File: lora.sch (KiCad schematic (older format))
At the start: 30 parts

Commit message: minor updates
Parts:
- removed J?: Program, symbol Connector_Generic:Conn_01x04
- removed U?: AZ1117-3.3, symbol Regulator_Linear:AZ1117-3.3
- added C?: 12p, Capacitor_SMD:C_0603_1608Metric, symbol Device:C_Small
- added J?: Temp, symbol Connector_Generic:Conn_01x03
- added R? (x2): 10k, symbol Device:R_Small
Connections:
- net labels added: RTC_IRQ
- wire segments 22 -> 31
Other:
- note added: "1.8V - 3.9V"
- note added: "1.8V - 5.5V"
- note added: "3.0V - 3.6V"
- note added: "3.5V Buck converter > 2.5A ! Not needed in battery mode!"
- note added: "SIM800 requires up to 2A in burst mode and 3.4V to 4.4V"
- note added: "UBLOX Neo 6: 2.7 - 3.6V"
- note removed: "Achtung 3.3V laut Datenblatt nicht ausreichend. \n"
- note removed: "Brauchen wir die anderen DIO1-5 wirklich nicht?"
- note removed: "Eingang Edge Interruptfähig?"
- note removed: "Ist 32D wirkich der Richtige? \nDa gibt es auch noch andere Endbuchstaben."
- moved on the sheet: J?

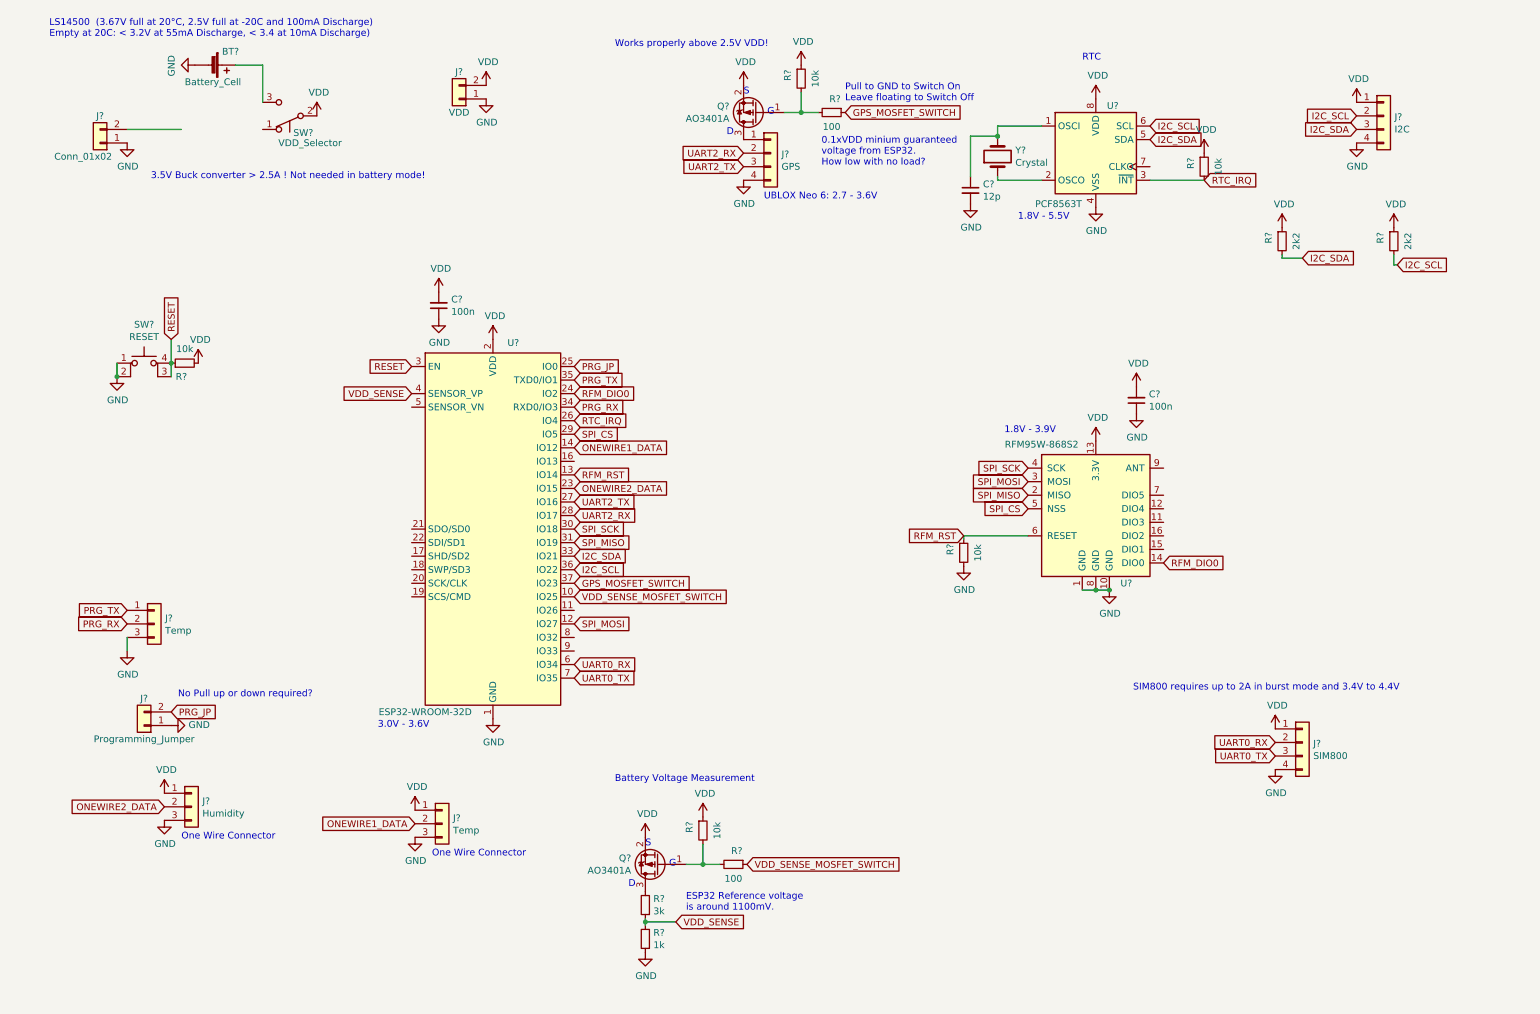
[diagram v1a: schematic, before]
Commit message: finished dc dc power supply.
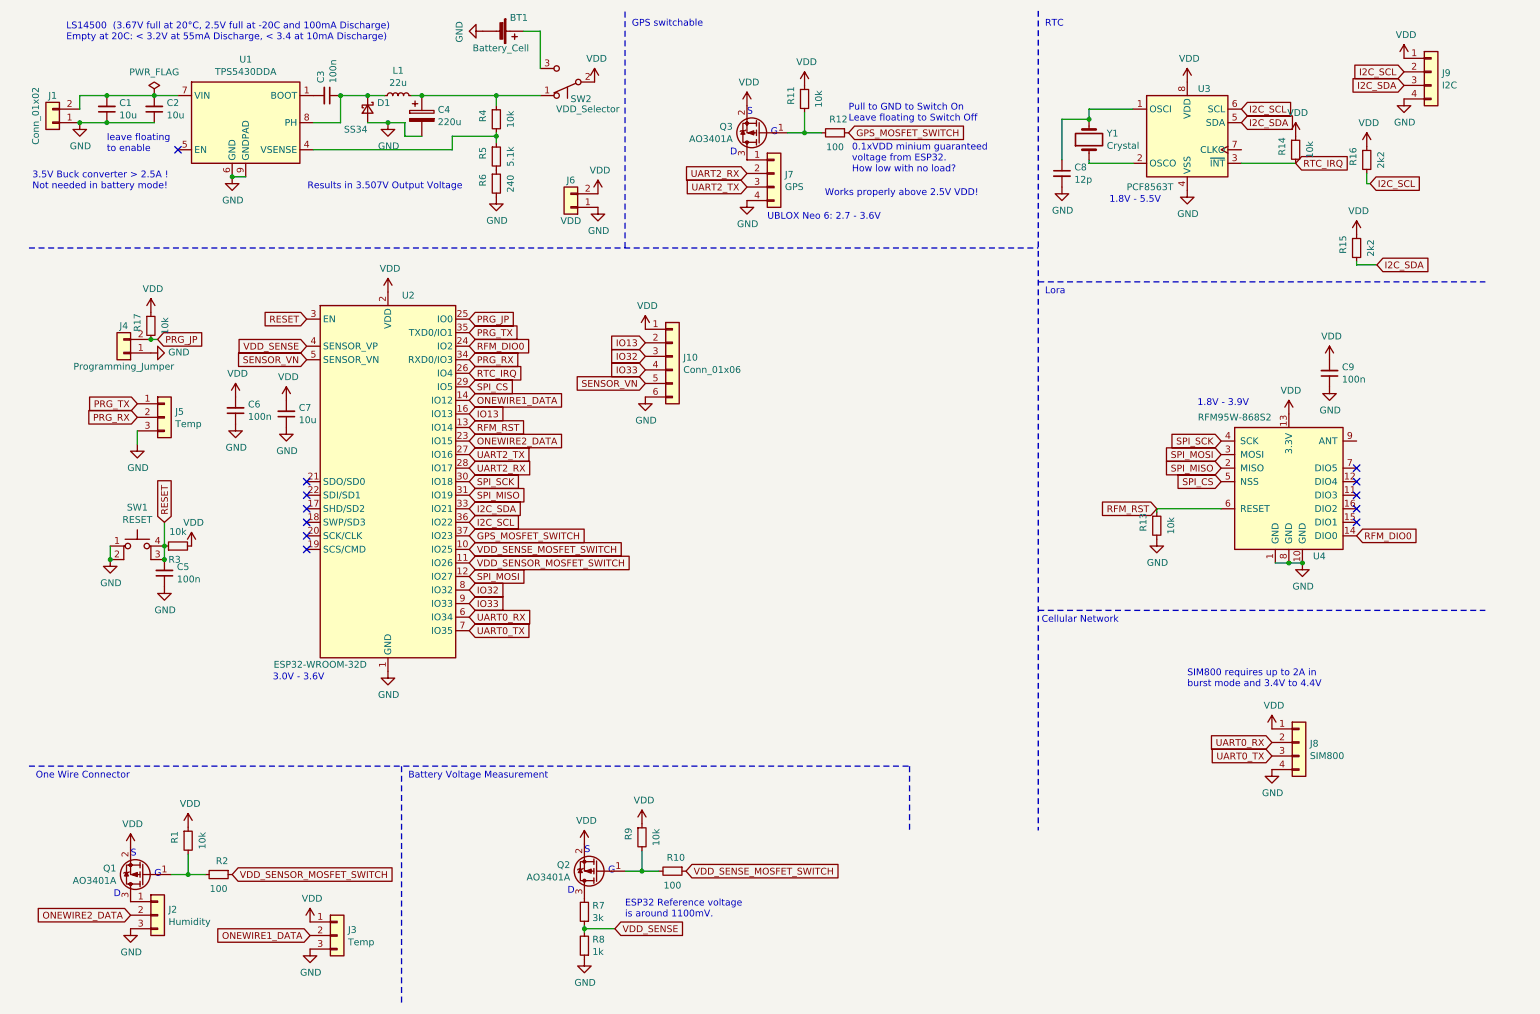
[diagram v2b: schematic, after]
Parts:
- added C1, C2, C7: 10u, symbol Device:C_Small
- added C3, C5: 100n, symbol Device:C_Small
- added C4: 220u, Capacitor_SMD:CP_Elec_6.3x7.7, symbol Device:CP
- added D1: SS34, symbol Device:D_Schottky_Small
- added J10: Conn_01x06, symbol Connector_Generic:Conn_01x06
- added L1: 22u, symbol Device:L_Small
- added Q1: AO3401A, Package_TO_SOT_SMD:SOT-23, symbol Transistor_FET:AO3401A
- added R1, R17, R4: 10k, symbol Device:R_Small
- added R2: 100, symbol Device:R_Small
- added R5: 5.1k, Resistor_SMD:R_0603_1608Metric, symbol Device:R_Small
- added R6: 240, Resistor_SMD:R_0603_1608Metric, symbol Device:R_Small
- added U1: TPS5430DDA, Package_SO:TI_SO-PowerPAD-8_ThermalVias, symbol Regulator_Switching:TPS5430DDA
- gave numbers to parts that had none: 32
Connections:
- net labels added: IO13, IO32, IO33, SENSOR_VN, VDD_SENSOR_MOSFET_SWITCH
- wire segments 31 -> 58
- no-connect marks 0 -> 12
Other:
- note added: "3.5V Buck converter > 2.5A !\nNot needed in battery mode!"
- note added: "Cellular Network"
- note added: "GPS switchable"
- note added: "Lora"
- note added: "Results in 3.507V Output Voltage"
- note added: "SIM800 requires up to 2A in \nburst mode and 3.4V to 4.4V"
- note added: "leave floating\nto enable"
- note removed: "3.5V Buck converter > 2.5A ! Not needed in battery mode!"
- note removed: "No Pull up or down required?"
- note removed: "SIM800 requires up to 2A in burst mode and 3.4V to 4.4V"
- moved on the sheet: BT1, C6, C8, C9, J1, J2, J3, J4, J5, J6, J7, J8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

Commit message: nothing major
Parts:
- added J11: Conn_Coaxial, symbol Connector:Conn_Coaxial
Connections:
- net GND: now also J11.2 (Ext)
- net at U4.9 (ANT): now also J11.1 (In)
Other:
- note added: "SMA or just a\nsimple short wire"
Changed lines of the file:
@@
 	1    0    0    -1
 $EndComp
+$Comp
+L Connector:Conn_Coaxial J11
+U 1 1 5FC31EE2
+P 10475 3650
+F 0 "J11" H 10575 3625 50  0000 L CNN
+F 1 "Conn_Coaxial" H 10575 3534 50  0000 L CNN
+F 2 "" H 10475 3650 50  0001 C CNN
+F 3 " ~" H 10475 3650 50  0001 C CNN
+	1    10475 3650
+	1    0    0    -1
+$EndComp
+$Comp
+L power:GND #PWR0146
+U 1 1 5FC3451D
+P 10475 3850
+F 0 "#PWR0146" H 10475 3600 50  0001 C CNN
+F 1 "GND" H 10480 3677 50  0000 C CNN
+F 2 "" H 10475 3850 50  0001 C CNN
+F 3 "" H 10475 3850 50  0001 C CNN
+	1    10475 3850
+	1    0    0    -1
+$EndComp
+Text Notes 10275 3500 0    50   ~ 0
+SMA or just a\nsimple short wire
 $EndSCHEMATC

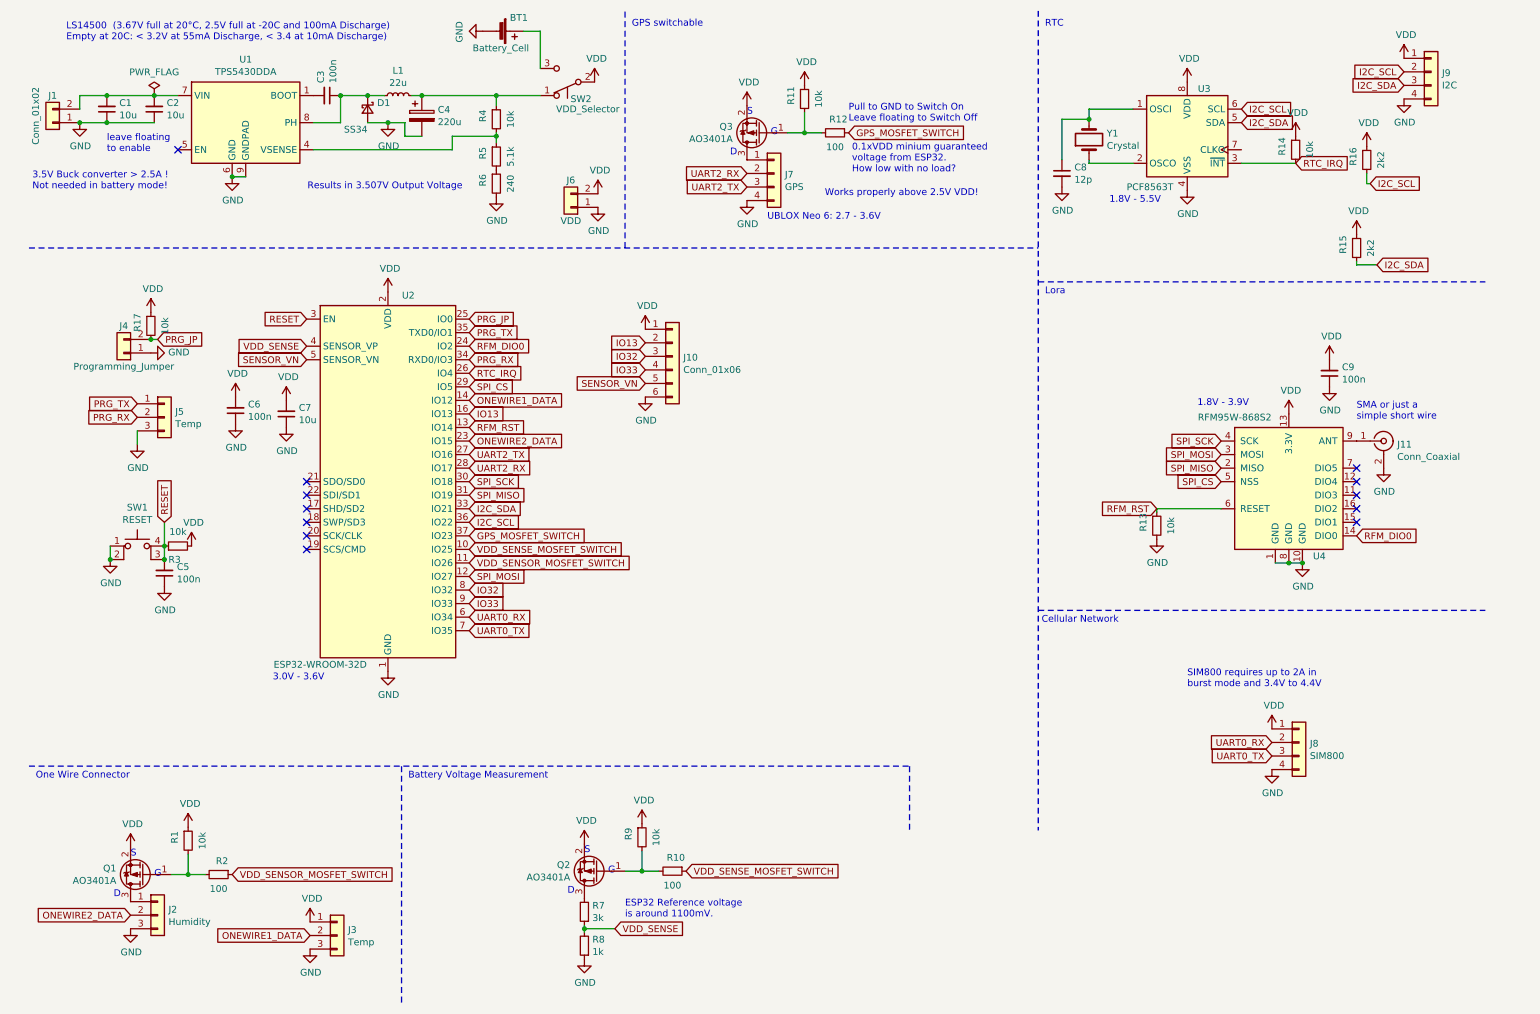
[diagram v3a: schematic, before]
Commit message: removed RTC, added 32KHZ crystal to esp32.
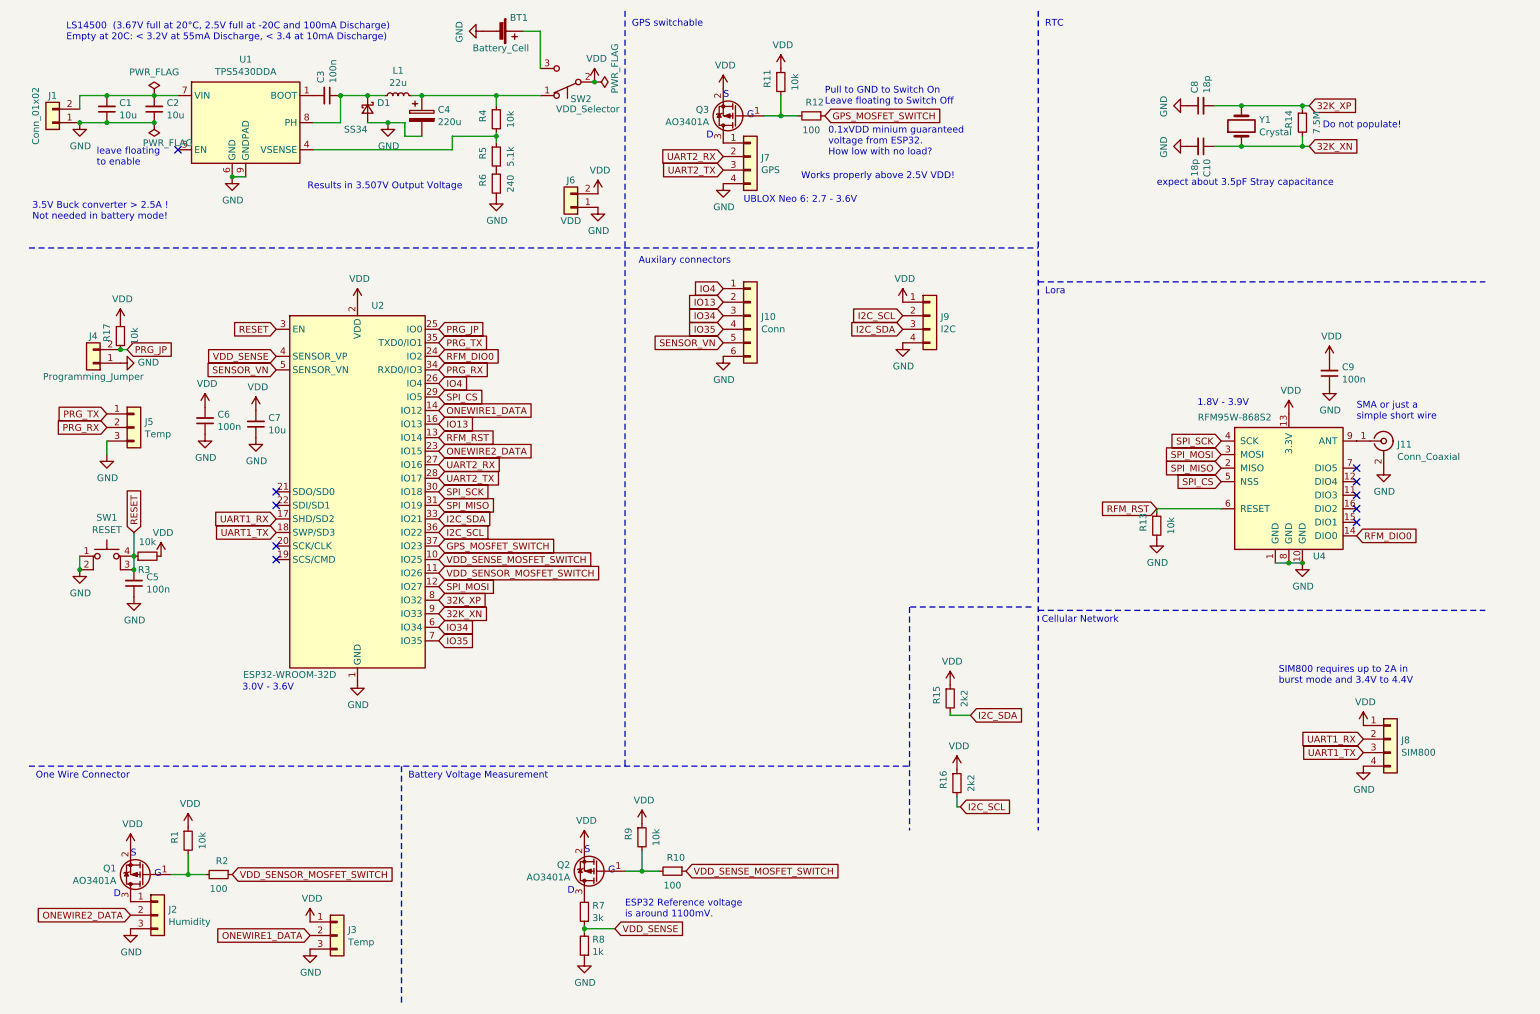
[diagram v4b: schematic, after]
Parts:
- removed U3: PCF8563T, Package_SO:SOIC-8_3.9x4.9mm_P1.27mm, symbol Timer_RTC:PCF8563T
- added C10: 18p, Capacitor_SMD:C_0603_1608Metric, symbol Device:C_Small
- C8: value 12p -> 18p; LCSC C38523 -> C1647
- J10: value Conn_01x06 -> Conn
- R14: value 10k -> 7.5M; footprint (none) -> Resistor_SMD:R_0603_1608Metric
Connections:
- net GND: now also C8.1, C10.2; no longer C8.2
- net UART2_RX: now also U2.27 (IO16); no longer U2.28 (IO17)
- net UART2_TX: now also U2.28 (IO17); no longer U2.27 (IO16)
- net VDD: no longer J10.1 (Pin_1), R14.1
- net UART1_RX: now reaches U2.17 (SHD/SD2)
- net UART1_RX: now also J8.2 (Pin_2)
- net UART1_TX: now reaches U2.18 (SWP/SD3)
- net UART1_TX: now also J8.3 (Pin_3)
- net 32K_XP: now reaches Y1.2
- net 32K_XP: now also C8.2, R14.1, U2.8 (IO32); no longer C8.1
- net 32K_XN: now reaches Y1.1
- net 32K_XN: now also R14.2, U2.9 (IO33), C10.1
- net IO32 renamed IO34
- net IO34: now also U2.6 (IO34); no longer U2.8 (IO32)
- net IO33 renamed IO35
- net IO35: now also U2.7 (IO35); no longer U2.9 (IO33)
- net RTC_IRQ renamed IO4
- net IO4: now also J10.1 (Pin_1); no longer R14.2
- removed net UART0_RX: J8.2 (Pin_2), U2.6 (IO34)
- removed net UART0_TX: J8.3 (Pin_3), U2.7 (IO35)
- no-connect marks 12 -> 10
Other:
- note added: "Auxilary connectors"
- note added: "Do not populate!"
- note added: "expect about 3.5pF Stray capacitance"
- note removed: "1.8V - 5.5V"
- moved on the sheet: C5, C6, C7, J10, J4, J5, J7, J8, J9, Q3, R11, R12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

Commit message: added reverse polarity protection.
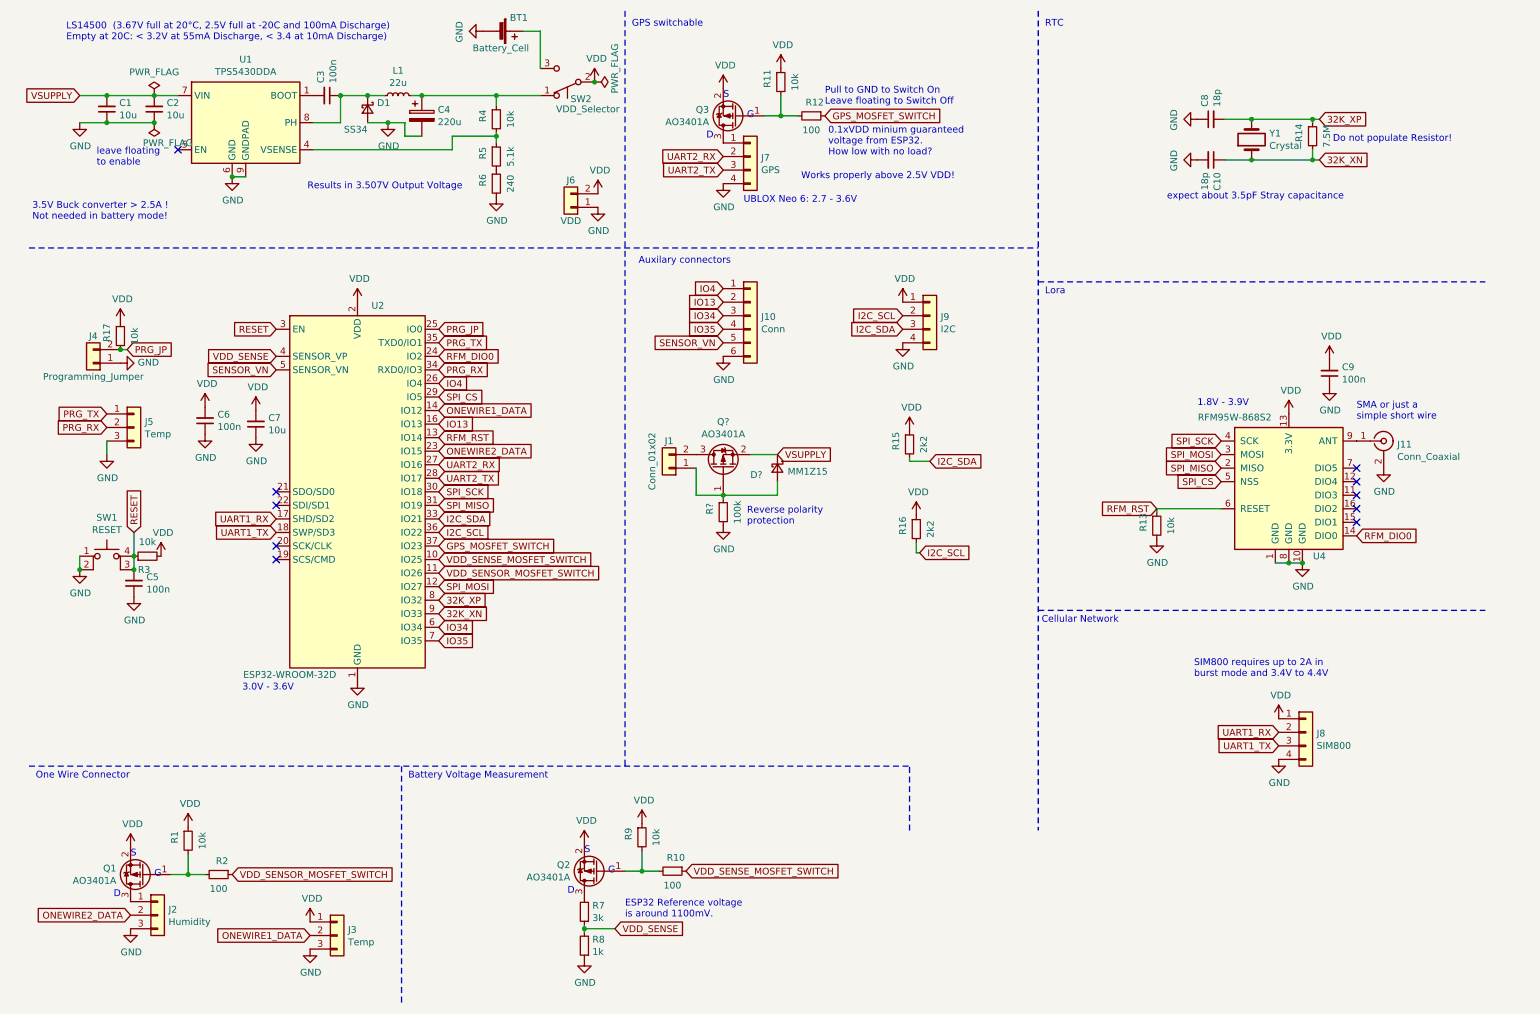
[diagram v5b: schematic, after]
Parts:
- added D?: MM1Z15, symbol Device:D_Schottky_Small
- added Q?: AO3401A, Package_TO_SOT_SMD:SOT-23, symbol Transistor_FET:AO3401A
- added R?: 100k, symbol Device:R_Small
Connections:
- net GND: now also R?.2; no longer J1.1 (Pin_1)
- net VSUPPLY: now reaches C1.2, C2.2, U1.7 (VIN)
- net VSUPPLY: now also D?.1 (K), Q?.2 (S); no longer J1.2 (Pin_2)
- new net: D?.2 (A), J1.1 (Pin_1), Q?.1 (G), R?.1
- new net: J1.2 (Pin_2), Q?.3 (D)
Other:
- note added: "Do not populate Resistor!"
- note added: "Reverse polarity \nprotection"
- note removed: "Do not populate!"
- moved on the sheet: C10, C8, J1, J8, R14, R15, R16, Y1
